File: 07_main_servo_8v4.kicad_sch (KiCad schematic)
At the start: 22 parts, among them J17 8.4 V TEST / AUX OUT, U11 TPS54560BDDA

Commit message: Complete pre-PCB electrical and safety audit
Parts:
- removed C59: 220 uF 16 V LOW ESR, Capacitor_THT:CP_Radial_D8.0mm_P3.50mm, symbol Device:C_Polarized
- added C59, C63, C66: 22 uF 25 V X7R, Capacitor_SMD:C_1210_3225Metric, symbol Device:C
- added TP60: ACT_VBAT, TestPoint:TestPoint_Loop_D2.50mm_Drill1.0mm, symbol Connector:TestPoint
- added TP61: ACTUATOR_ENABLE, TestPoint:TestPoint_Loop_D2.50mm_Drill1.0mm, symbol Connector:TestPoint
- added TP62: MAIN_SERVO_8V4, TestPoint:TestPoint_Loop_D2.50mm_Drill1.0mm, symbol Connector:TestPoint
- added TP63: GND, TestPoint:TestPoint_Loop_D2.50mm_Drill1.0mm, symbol Connector:TestPoint
- C57: value 4.7 nF -> 5.6 nF
- C60: value 1 uF 16 V -> 22 uF 25 V X7R; footprint Capacitor_SMD:C_0805_2012Metric -> Capacitor_SMD:C_1210_3225Metric
- C61: value 1000 uF 16 V LOW ESR -> 220 uF 16 V LOW ESR; footprint Capacitor_THT:CP_Radial_D10.0mm_P5.00mm -> Capacitor_THT:CP_Radial_D8.0mm_P3.50mm
- F4: value 5 A MAIN SERVO -> 5 A MINI BLADE MAIN SERVO; footprint Fuse:Fuse_1206_3216Metric -> Fuse:Fuseholder_Blade_Mini_Keystone_3568
- R109: value 866 k 1% -> 96.9 k 1%
- R110: value 90.9 k 1% -> 10.2 k 1%
- R111: value 10.2 k -> 17.8 k 1%
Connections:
- net GND: now also C59.2, C63.2, C66.2, TP63.1
- net MAIN8_RAW: now also C59.1, C63.1, C66.1
- net MAIN_SERVO_8V4: now also TP62.1
- net VBAT_SW renamed ACT_VBAT
- net ACT_VBAT: now also TP60.1; no longer U11.3 (EN)
- new net ACTUATOR_ENABLE: TP61.1, U11.3 (EN)
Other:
- note added: "U11 uses 96.9 k / 10.2 k feedback resistors for approximately 8.40 V. J12 is the only servo powered from this rail."
- note removed: "U11 uses 866 k / 90.9 k feedback resistors for approximately 8.42 V. J12 is the only servo powered from this rail."

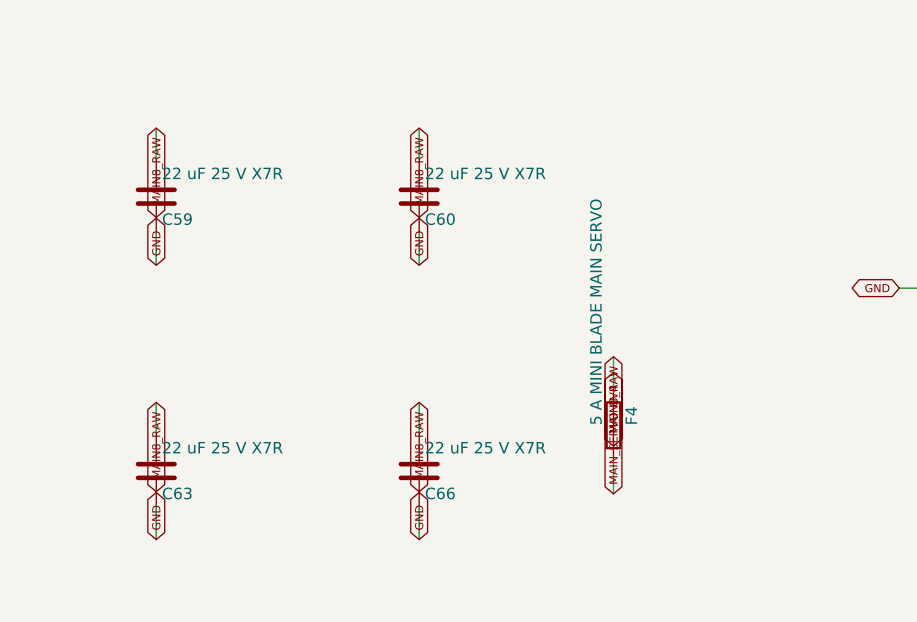
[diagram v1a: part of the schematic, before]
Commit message: Select robust 8.4V rail output capacitors
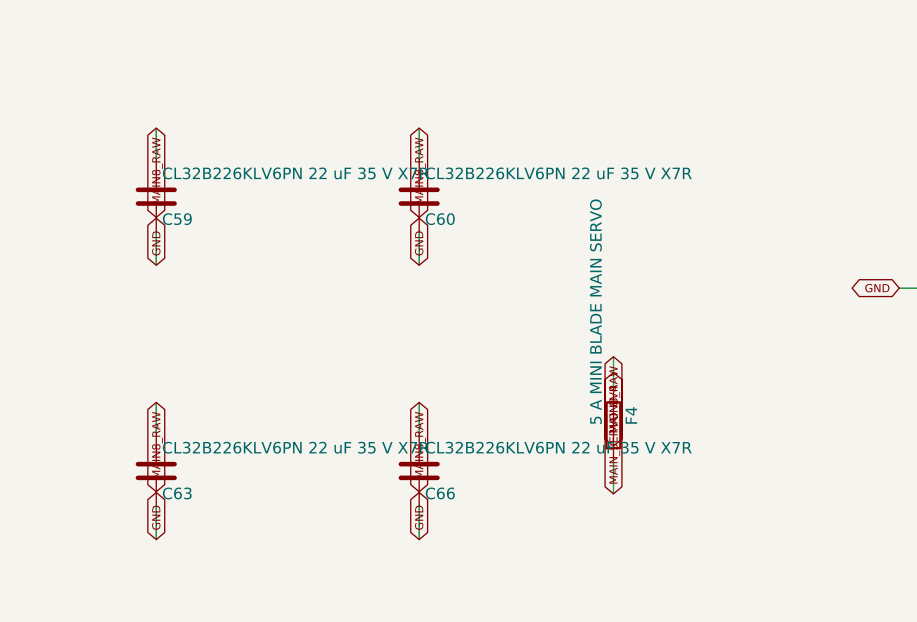
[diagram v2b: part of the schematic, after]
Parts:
- C59, C60, C63, C66: value 22 uF 25 V X7R -> CL32B226KLV6PN 22 uF 35 V X7R
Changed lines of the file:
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@@
 		(instances
 			(project "pickleball_robot_controller"
-				(path "/a6893b11-d9bc-4a80-990f-65dd0b889366/d5ba1fc4-6759-4cd9-852f-e10138c73d3f"
+				(path "/e446fdd7-1073-4cff-9c2d-f103458c4377/b362603b-535e-4a9f-b321-df392e31a60a"
 					(reference "U11")
 					(unit 1)
@@
 		(instances
 			(project "pickleball_robot_controller"
-				(path "/a6893b11-d9bc-4a80-990f-65dd0b889366/d5ba1fc4-6759-4cd9-852f-e10138c73d3f"
+				(path "/e446fdd7-1073-4cff-9c2d-f103458c4377/b362603b-535e-4a9f-b321-df392e31a60a"
 					(reference "C52")
 					(unit 1)
@@
 		(instances
 			(project "pickleball_robot_controller"
-				(path "/a6893b11-d9bc-4a80-990f-65dd0b889366/d5ba1fc4-6759-4cd9-852f-e10138c73d3f"
+				(path "/e446fdd7-1073-4cff-9c2d-f103458c4377/b362603b-535e-4a9f-b321-df392e31a60a"
 					(reference "D11")
 					(unit 1)
@@
 		(instances
 			(project "pickleball_robot_controller"
-				(path "/a6893b11-d9bc-4a80-990f-65dd0b889366/d5ba1fc4-6759-4cd9-852f-e10138c73d3f"
+				(path "/e446fdd7-1073-4cff-9c2d-f103458c4377/b362603b-535e-4a9f-b321-df392e31a60a"
 					(reference "L4")
 					(unit 1)
@@
 		(instances
 			(project "pickleball_robot_controller"
-				(path "/a6893b11-d9bc-4a80-990f-65dd0b889366/d5ba1fc4-6759-4cd9-852f-e10138c73d3f"
+				(path "/e446fdd7-1073-4cff-9c2d-f103458c4377/b362603b-535e-4a9f-b321-df392e31a60a"
 					(reference "C53")
 					(unit 1)
@@
 		(instances
 			(project "pickleball_robot_controller"
-				(path "/a6893b11-d9bc-4a80-990f-65dd0b889366/d5ba1fc4-6759-4cd9-852f-e10138c73d3f"
+				(path "/e446fdd7-1073-4cff-9c2d-f103458c4377/b362603b-535e-4a9f-b321-df392e31a60a"
 					(reference "C54")
 					(unit 1)
@@
 		(instances
 			(project "pickleball_robot_controller"
-				(path "/a6893b11-d9bc-4a80-990f-65dd0b889366/d5ba1fc4-6759-4cd9-852f-e10138c73d3f"
+				(path "/e446fdd7-1073-4cff-9c2d-f103458c4377/b362603b-535e-4a9f-b321-df392e31a60a"
 					(reference "C55")
 					(unit 1)
@@
 		(instances
 			(project "pickleball_robot_controller"
-				(path "/a6893b11-d9bc-4a80-990f-65dd0b889366/d5ba1fc4-6759-4cd9-852f-e10138c73d3f"
+				(path "/e446fdd7-1073-4cff-9c2d-f103458c4377/b362603b-535e-4a9f-b321-df392e31a60a"
 					(reference "C56")
 					(unit 1)
@@
 		(instances
 			(project "pickleball_robot_controller"
-				(path "/a6893b11-d9bc-4a80-990f-65dd0b889366/d5ba1fc4-6759-4cd9-852f-e10138c73d3f"
+				(path "/e446fdd7-1073-4cff-9c2d-f103458c4377/b362603b-535e-4a9f-b321-df392e31a60a"
 					(reference "R108")
 					(unit 1)
@@
 		(instances
 			(project "pickleball_robot_controller"
-				(path "/a6893b11-d9bc-4a80-990f-65dd0b889366/d5ba1fc4-6759-4cd9-852f-e10138c73d3f"
+				(path "/e446fdd7-1073-4cff-9c2d-f103458c4377/b362603b-535e-4a9f-b321-df392e31a60a"
 					(reference "R109")
 					(unit 1)
@@
 		(instances
 			(project "pickleball_robot_controller"
-				(path "/a6893b11-d9bc-4a80-990f-65dd0b889366/d5ba1fc4-6759-4cd9-852f-e10138c73d3f"
+				(path "/e446fdd7-1073-4cff-9c2d-f103458c4377/b362603b-535e-4a9f-b321-df392e31a60a"
 					(reference "R110")
 					(unit 1)
@@
 		(instances
 			(project "pickleball_robot_controller"
-				(path "/a6893b11-d9bc-4a80-990f-65dd0b889366/d5ba1fc4-6759-4cd9-852f-e10138c73d3f"
+				(path "/e446fdd7-1073-4cff-9c2d-f103458c4377/b362603b-535e-4a9f-b321-df392e31a60a"
 					(reference "R111")
 					(unit 1)
@@
 		(instances
 			(project "pickleball_robot_controller"
-				(path "/a6893b11-d9bc-4a80-990f-65dd0b889366/d5ba1fc4-6759-4cd9-852f-e10138c73d3f"
+				(path "/e446fdd7-1073-4cff-9c2d-f103458c4377/b362603b-535e-4a9f-b321-df392e31a60a"
 					(reference "C57")
 					(unit 1)
@@
 		(instances
 			(project "pickleball_robot_controller"
-				(path "/a6893b11-d9bc-4a80-990f-65dd0b889366/d5ba1fc4-6759-4cd9-852f-e10138c73d3f"
+				(path "/e446fdd7-1073-4cff-9c2d-f103458c4377/b362603b-535e-4a9f-b321-df392e31a60a"
 					(reference "C58")
 					(unit 1)
@@
 			)
 		)
-		(property "Value" "22 uF 25 V X7R"
+		(property "Value" "CL32B226KLV6PN 22 uF 35 V X7R"
 			(at 280.035 46.99 0.0000)
 			(effects
@@
 		(instances
 			(project "pickleball_robot_controller"
-				(path "/a6893b11-d9bc-4a80-990f-65dd0b889366/d5ba1fc4-6759-4cd9-852f-e10138c73d3f"
+				(path "/e446fdd7-1073-4cff-9c2d-f103458c4377/b362603b-535e-4a9f-b321-df392e31a60a"
 					(reference "C59")
 					(unit 1)
@@
 			)
 		)
-		(property "Value" "22 uF 25 V X7R"
+		(property "Value" "CL32B226KLV6PN 22 uF 35 V X7R"
 			(at 309.245 46.99 0.0000)
 			(effects
@@
 		(instances
 			(project "pickleball_robot_controller"
-				(path "/a6893b11-d9bc-4a80-990f-65dd0b889366/d5ba1fc4-6759-4cd9-852f-e10138c73d3f"
+				(path "/e446fdd7-1073-4cff-9c2d-f103458c4377/b362603b-535e-4a9f-b321-df392e31a60a"
 					(reference "C60")
 					(unit 1)
@@
 			)
 		)
-		(property "Value" "22 uF 25 V X7R"
+		(property "Value" "CL32B226KLV6PN 22 uF 35 V X7R"
 			(at 280.035 77.47 0.0000)
 			(effects
@@
 		(instances
 			(project "pickleball_robot_controller"
-				(path "/a6893b11-d9bc-4a80-990f-65dd0b889366/d5ba1fc4-6759-4cd9-852f-e10138c73d3f"
+				(path "/e446fdd7-1073-4cff-9c2d-f103458c4377/b362603b-535e-4a9f-b321-df392e31a60a"
 					(reference "C63")
 					(unit 1)
@@
 			)
 		)
-		(property "Value" "22 uF 25 V X7R"
+		(property "Value" "CL32B226KLV6PN 22 uF 35 V X7R"
 			(at 309.245 77.47 0.0000)
 			(effects
@@
 		(instances
 			(project "pickleball_robot_controller"
-				(path "/a6893b11-d9bc-4a80-990f-65dd0b889366/d5ba1fc4-6759-4cd9-852f-e10138c73d3f"
+				(path "/e446fdd7-1073-4cff-9c2d-f103458c4377/b362603b-535e-4a9f-b321-df392e31a60a"
 					(reference "C66")
 					(unit 1)
@@
 		(instances
 			(project "pickleball_robot_controller"
-				(path "/a6893b11-d9bc-4a80-990f-65dd0b889366/d5ba1fc4-6759-4cd9-852f-e10138c73d3f"
+				(path "/e446fdd7-1073-4cff-9c2d-f103458c4377/b362603b-535e-4a9f-b321-df392e31a60a"
 					(reference "F4")
 					(unit 1)
@@
 		(instances
 			(project "pickleball_robot_controller"
-				(path "/a6893b11-d9bc-4a80-990f-65dd0b889366/d5ba1fc4-6759-4cd9-852f-e10138c73d3f"
+				(path "/e446fdd7-1073-4cff-9c2d-f103458c4377/b362603b-535e-4a9f-b321-df392e31a60a"
 					(reference "D12")
 					(unit 1)
@@
 		(instances
 			(project "pickleball_robot_controller"
-				(path "/a6893b11-d9bc-4a80-990f-65dd0b889366/d5ba1fc4-6759-4cd9-852f-e10138c73d3f"
+				(path "/e446fdd7-1073-4cff-9c2d-f103458c4377/b362603b-535e-4a9f-b321-df392e31a60a"
 					(reference "C61")
 					(unit 1)
@@
 		(instances
 			(project "pickleball_robot_controller"
-				(path "/a6893b11-d9bc-4a80-990f-65dd0b889366/d5ba1fc4-6759-4cd9-852f-e10138c73d3f"
+				(path "/e446fdd7-1073-4cff-9c2d-f103458c4377/b362603b-535e-4a9f-b321-df392e31a60a"
 					(reference "J17")
 					(unit 1)
@@
 		(instances
 			(project "pickleball_robot_controller"
-				(path "/a6893b11-d9bc-4a80-990f-65dd0b889366/d5ba1fc4-6759-4cd9-852f-e10138c73d3f"
+				(path "/e446fdd7-1073-4cff-9c2d-f103458c4377/b362603b-535e-4a9f-b321-df392e31a60a"
 					(reference "R112")
 					(unit 1)
@@
 		(instances
 			(project "pickleball_robot_controller"
-				(path "/a6893b11-d9bc-4a80-990f-65dd0b889366/d5ba1fc4-6759-4cd9-852f-e10138c73d3f"
+				(path "/e446fdd7-1073-4cff-9c2d-f103458c4377/b362603b-535e-4a9f-b321-df392e31a60a"
 					(reference "D13")
 					(unit 1)
@@
 		(instances
 			(project "pickleball_robot_controller"
-				(path "/a6893b11-d9bc-4a80-990f-65dd0b889366/d5ba1fc4-6759-4cd9-852f-e10138c73d3f"
+				(path "/e446fdd7-1073-4cff-9c2d-f103458c4377/b362603b-535e-4a9f-b321-df392e31a60a"
 					(reference "#FLG08")
 					(unit 1)
@@
 		(instances
 			(project "pickleball_robot_controller"
-				(path "/a6893b11-d9bc-4a80-990f-65dd0b889366/d5ba1fc4-6759-4cd9-852f-e10138c73d3f"
+				(path "/e446fdd7-1073-4cff-9c2d-f103458c4377/b362603b-535e-4a9f-b321-df392e31a60a"
 					(reference "TP60")
 					(unit 1)
@@
 		(instances
 			(project "pickleball_robot_controller"
-				(path "/a6893b11-d9bc-4a80-990f-65dd0b889366/d5ba1fc4-6759-4cd9-852f-e10138c73d3f"
+				(path "/e446fdd7-1073-4cff-9c2d-f103458c4377/b362603b-535e-4a9f-b321-df392e31a60a"
 					(reference "TP61")
 					(unit 1)
@@
 		(instances
 			(project "pickleball_robot_controller"
-				(path "/a6893b11-d9bc-4a80-990f-65dd0b889366/d5ba1fc4-6759-4cd9-852f-e10138c73d3f"
+				(path "/e446fdd7-1073-4cff-9c2d-f103458c4377/b362603b-535e-4a9f-b321-df392e31a60a"
 					(reference "TP62")
 					(unit 1)
@@
 		(instances
 			(project "pickleball_robot_controller"
-				(path "/a6893b11-d9bc-4a80-990f-65dd0b889366/d5ba1fc4-6759-4cd9-852f-e10138c73d3f"
+				(path "/e446fdd7-1073-4cff-9c2d-f103458c4377/b362603b-535e-4a9f-b321-df392e31a60a"
 					(reference "TP63")
 					(unit 1)
@@
 	)
 	(sheet_instances
-		(path "/a6893b11-d9bc-4a80-990f-65dd0b889366/d5ba1fc4-6759-4cd9-852f-e10138c73d3f"
+		(path "/e446fdd7-1073-4cff-9c2d-f103458c4377/b362603b-535e-4a9f-b321-df392e31a60a"
 			(page "8")
 		)

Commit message: Correct critical controller schematic safety issues
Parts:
- added C70: DNP SNUBBER 1 nF, Capacitor_SMD:C_0805_2012Metric, symbol Device:C
- added R114: DNP SNUBBER 10 R, Resistor_SMD:R_0805_2012Metric, symbol Device:R
- C53, C54, C55, C56: value 2.2 uF 25 V -> 2.2 uF 25 V X7R
- C59, C60, C63, C66: value CL32B226KLV6PN 22 uF 35 V X7R -> 22 uF 35 V X7R
- C61: value 220 uF 16 V LOW ESR -> DNP OPTIONAL Panasonic EEU-FR1E221 220 uF 25 V; now not fitted
- D12: value SMBJ10A -> SMBJ10CA BIDIRECTIONAL
- TP60, TP62, TP63: footprint TestPoint:TestPoint_Loop_D2.50mm_Drill1.0mm -> TestPoint:TestPoint_Pad_D1.5mm; now left out of the parts list
- TP61: value ACTUATOR_ENABLE -> SERVO_POWER_ENABLE; footprint TestPoint:TestPoint_Loop_D2.50mm_Drill1.0mm -> TestPoint:TestPoint_Pad_D1.5mm; now left out of the parts list
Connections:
- net GND: now also D11.2 (A), D12.2 (A2), D13.1 (K), C70.2; no longer D11.1 (K), D12.1 (A1), D13.2 (A)
- net LED_MAIN8: now also D13.2 (A); no longer D13.1 (K)
- net MAIN8_SW: now also D11.1 (K), R114.1; no longer D11.2 (A)
- net MAIN_SERVO_8V4: now also D12.1 (A1); no longer D12.2 (A2)
- net ACTUATOR_ENABLE renamed SERVO_POWER_ENABLE
- new net MAIN8_SNUB: C70.1, R114.2

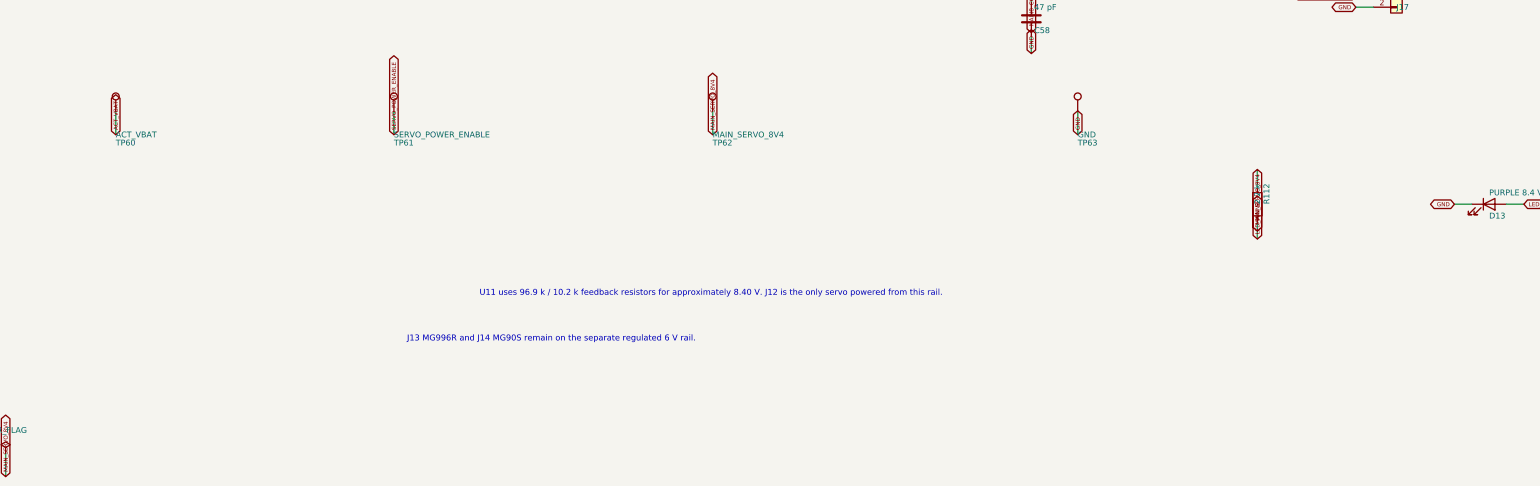
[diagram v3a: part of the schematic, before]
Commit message: Add whole-system battery cutoff and hardened servo interfaces
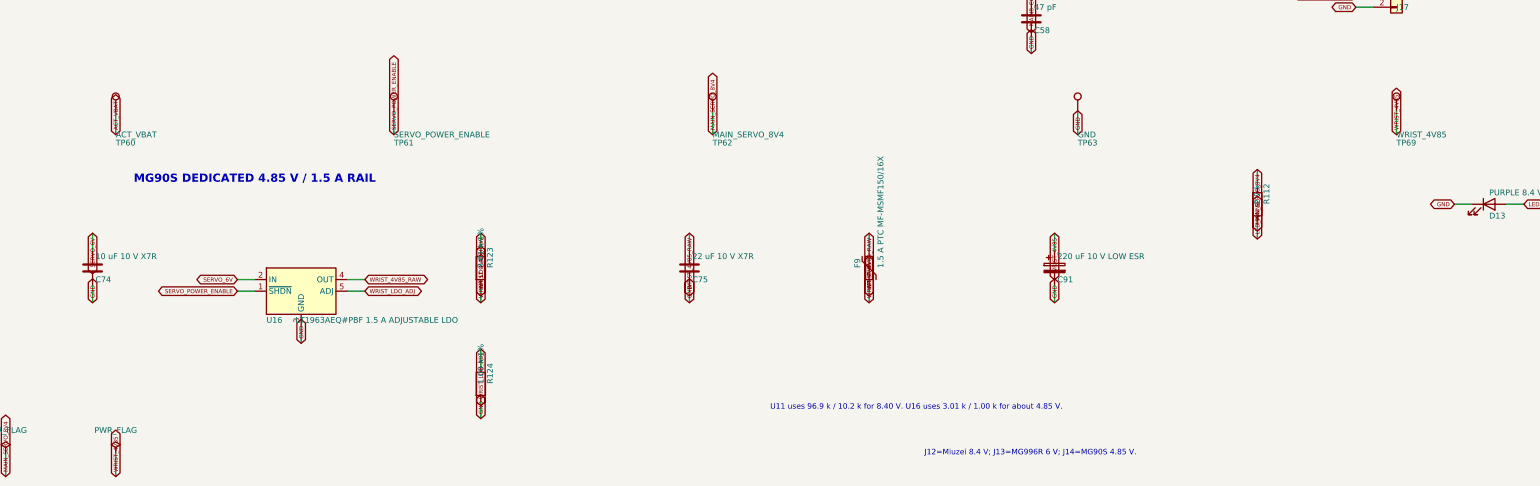
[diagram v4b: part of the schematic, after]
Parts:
- added C74: 10 uF 10 V X7R, Capacitor_SMD:C_0805_2012Metric, symbol Device:C
- added C75: 22 uF 10 V X7R, Capacitor_SMD:C_1210_3225Metric, symbol Device:C
- added C91: 220 uF 10 V LOW ESR, Capacitor_THT:CP_Radial_D8.0mm_P3.50mm, symbol Device:C_Polarized
- added F9: 1.5 A PTC MF-MSMF150/16X, Fuse:Fuse_1812_4532Metric, symbol Device:Polyfuse
- added R123: 3.01 k 1%, Resistor_SMD:R_0805_2012Metric, symbol Device:R
- added R124: 1.00 k 1%, Resistor_SMD:R_0805_2012Metric, symbol Device:R
- added TP69: WRIST_4V85, TestPoint:TestPoint_Pad_D1.5mm, symbol Connector:TestPoint
- added U16: LT1963AEQ#PBF 1.5 A ADJUSTABLE LDO, Package_TO_SOT_SMD:TO-263-5_TabPin3, symbol Regulator_Linear:LT1963AEQ
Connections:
- net GND: now also C74.2, C75.2, C91.2, R124.2, U16.3 (GND)
- net SERVO_POWER_ENABLE: now also U16.1 (~{SHDN})
- new net SERVO_6V: C74.1, U16.2 (IN)
- new net WRIST_4V85: C91.1, F9.2, TP69.1
- new net WRIST_4V85_RAW: C75.1, F9.1, R123.1, U16.4 (OUT)
- new net WRIST_LDO_ADJ: R123.2, R124.1, U16.5 (ADJ)
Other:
- note added: "J12=Miuzei 8.4 V; J13=MG996R 6 V; J14=MG90S 4.85 V."
- note added: "MG90S DEDICATED 4.85 V / 1.5 A RAIL"
- note added: "U11 uses 96.9 k / 10.2 k for 8.40 V. U16 uses 3.01 k / 1.00 k for about 4.85 V."
- note removed: "J13 MG996R and J14 MG90S remain on the separate regulated 6 V rail."
- note removed: "U11 uses 96.9 k / 10.2 k feedback resistors for approximately 8.40 V. J12 is the only servo powered from this rail."
- title: Miuzei Main-Swing Servo 8.4 V Power Rail -> Miuzei 8.4 V and MG90S 4.85 V Power Rails
